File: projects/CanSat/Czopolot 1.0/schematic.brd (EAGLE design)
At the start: 35.6 x 50.8 mm, 12 parts

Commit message: Work work..
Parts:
- moved JP1 2.54 mm to (3.81, -48.3)
- moved JP2 2.54 mm to (36.8, -48.3)
- moved Q1 2.54 mm to (29.2, -49.5)
- moved Q2 2.54 mm to (11.4, -49.5)
- moved R1 2.54 mm to (29.2, -41.9)
- moved R2 2.54 mm to (11.4, -41.9)
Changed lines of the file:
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@@
 <?xml version="1.0" encoding="utf-8"?>
 <!DOCTYPE eagle SYSTEM "eagle.dtd">
-<eagle version="9.5.2">
+<eagle version="9.5.1">
 <drawing>
 <settings>
@@
 <element name="U$3" library="SobieskiSat2" package="MODULE_MPU9250" value="MPU9250" x="20.32" y="-8.001" smashed="yes" rot="R270"/>
 <element name="U$4" library="SobieskiSat2" package="MODULE_BMP280" value="BMP280" x="15.24" y="-28.829" smashed="yes" rot="R90"/>
-<element name="R1" library="rcl" library_urn="urn:adsk.eagle:library:334" package="0207/10" package3d_urn="urn:adsk.eagle:package:23491/2" value="" x="26.67" y="-41.91" smashed="yes" rot="R180">
-<attribute name="NAME" x="29.718" y="-43.434" size="1.27" layer="25" ratio="10" rot="R180"/>
-<attribute name="POPULARITY" value="81" x="26.67" y="-41.91" size="1.778" layer="27" rot="R180" display="off"/>
-<attribute name="SPICEPREFIX" value="R" x="26.67" y="-41.91" size="1.778" layer="27" rot="R180" display="off"/>
-<attribute name="VALUE" x="28.9306" y="-41.275" size="1.27" layer="27" ratio="10" rot="R180"/>
-</element>
-<element name="R2" library="rcl" library_urn="urn:adsk.eagle:library:334" package="0207/10" package3d_urn="urn:adsk.eagle:package:23491/2" value="" x="8.89" y="-41.91" smashed="yes" rot="R180">
-<attribute name="NAME" x="11.938" y="-43.434" size="1.27" layer="25" ratio="10" rot="R180"/>
-<attribute name="POPULARITY" value="81" x="8.89" y="-41.91" size="1.778" layer="27" rot="R180" display="off"/>
-<attribute name="SPICEPREFIX" value="R" x="8.89" y="-41.91" size="1.778" layer="27" rot="R180" display="off"/>
-<attribute name="VALUE" x="11.1506" y="-41.275" size="1.27" layer="27" ratio="10" rot="R180"/>
-</element>
-<element name="Q1" library="adafruit" library_urn="urn:adsk.eagle:library:420" package="TO220V" package3d_urn="urn:adsk.eagle:package:6240882/1" value="" x="26.67" y="-49.53" smashed="yes" rot="R180">
-<attribute name="NAME" x="31.75" y="-43.4848" size="1.27" layer="25" ratio="10" rot="R180"/>
-<attribute name="VALUE" x="31.75" y="-41.91" size="1.27" layer="27" ratio="10" rot="R180"/>
-</element>
-<element name="Q2" library="adafruit" library_urn="urn:adsk.eagle:library:420" package="TO220V" package3d_urn="urn:adsk.eagle:package:6240882/1" value="" x="8.89" y="-49.53" smashed="yes" rot="R180">
-<attribute name="NAME" x="13.97" y="-43.4848" size="1.27" layer="25" ratio="10" rot="R180"/>
-<attribute name="VALUE" x="13.97" y="-41.91" size="1.27" layer="27" ratio="10" rot="R180"/>
-</element>
-<element name="JP1" library="pinhead" library_urn="urn:adsk.eagle:library:325" package="1X02" package3d_urn="urn:adsk.eagle:package:22435/2" value="" x="1.27" y="-48.26" smashed="yes" rot="R90">
-<attribute name="NAME" x="-0.5588" y="-50.8762" size="1.27" layer="25" ratio="10" rot="R90"/>
-<attribute name="POPULARITY" value="98" x="1.27" y="-48.26" size="1.778" layer="27" rot="R90" display="off"/>
-<attribute name="VALUE" x="4.445" y="-50.8" size="1.27" layer="27" rot="R90"/>
-</element>
-<element name="JP2" library="pinhead" library_urn="urn:adsk.eagle:library:325" package="1X02" package3d_urn="urn:adsk.eagle:package:22435/2" value="" x="34.29" y="-48.26" smashed="yes" rot="R90">
-<attribute name="NAME" x="32.4612" y="-50.8762" size="1.27" layer="25" ratio="10" rot="R90"/>
-<attribute name="POPULARITY" value="98" x="34.29" y="-48.26" size="1.778" layer="27" rot="R90" display="off"/>
-<attribute name="VALUE" x="37.465" y="-50.8" size="1.27" layer="27" rot="R90"/>
+<element name="R1" library="rcl" library_urn="urn:adsk.eagle:library:334" package="0207/10" package3d_urn="urn:adsk.eagle:package:23491/2" value="" x="29.21" y="-41.91" smashed="yes" rot="R180">
+<attribute name="NAME" x="32.258" y="-43.434" size="1.27" layer="25" ratio="10" rot="R180"/>
+<attribute name="POPULARITY" value="81" x="29.21" y="-41.91" size="1.778" layer="27" rot="R180" display="off"/>
+<attribute name="SPICEPREFIX" value="R" x="29.21" y="-41.91" size="1.778" layer="27" rot="R180" display="off"/>
+<attribute name="VALUE" x="31.4706" y="-41.275" size="1.27" layer="27" ratio="10" rot="R180"/>
+</element>
+<element name="R2" library="rcl" library_urn="urn:adsk.eagle:library:334" package="0207/10" package3d_urn="urn:adsk.eagle:package:23491/2" value="" x="11.43" y="-41.91" smashed="yes" rot="R180">
+<attribute name="NAME" x="14.478" y="-43.434" size="1.27" layer="25" ratio="10" rot="R180"/>
+<attribute name="POPULARITY" value="81" x="11.43" y="-41.91" size="1.778" layer="27" rot="R180" display="off"/>
+<attribute name="SPICEPREFIX" value="R" x="11.43" y="-41.91" size="1.778" layer="27" rot="R180" display="off"/>
+<attribute name="VALUE" x="13.6906" y="-41.275" size="1.27" layer="27" ratio="10" rot="R180"/>
+</element>
+<element name="Q1" library="adafruit" library_urn="urn:adsk.eagle:library:420" package="TO220V" package3d_urn="urn:adsk.eagle:package:6240882/1" value="" x="29.21" y="-49.53" smashed="yes" rot="R180">
+<attribute name="NAME" x="34.29" y="-43.4848" size="1.27" layer="25" ratio="10" rot="R180"/>
+<attribute name="VALUE" x="34.29" y="-41.91" size="1.27" layer="27" ratio="10" rot="R180"/>
+</element>
+<element name="Q2" library="adafruit" library_urn="urn:adsk.eagle:library:420" package="TO220V" package3d_urn="urn:adsk.eagle:package:6240882/1" value="" x="11.43" y="-49.53" smashed="yes" rot="R180">
+<attribute name="NAME" x="16.51" y="-43.4848" size="1.27" layer="25" ratio="10" rot="R180"/>
+<attribute name="VALUE" x="16.51" y="-41.91" size="1.27" layer="27" ratio="10" rot="R180"/>
+</element>
+<element name="JP1" library="pinhead" library_urn="urn:adsk.eagle:library:325" package="1X02" package3d_urn="urn:adsk.eagle:package:22435/2" value="" x="3.81" y="-48.26" smashed="yes" rot="R90">
+<attribute name="NAME" x="1.9812" y="-50.8762" size="1.27" layer="25" ratio="10" rot="R90"/>
+<attribute name="POPULARITY" value="98" x="3.81" y="-48.26" size="1.778" layer="27" rot="R90" display="off"/>
+<attribute name="VALUE" x="6.985" y="-50.8" size="1.27" layer="27" rot="R90"/>
+</element>
+<element name="JP2" library="pinhead" library_urn="urn:adsk.eagle:library:325" package="1X02" package3d_urn="urn:adsk.eagle:package:22435/2" value="" x="36.83" y="-48.26" smashed="yes" rot="R90">
+<attribute name="NAME" x="35.0012" y="-50.8762" size="1.27" layer="25" ratio="10" rot="R90"/>
+<attribute name="POPULARITY" value="98" x="36.83" y="-48.26" size="1.778" layer="27" rot="R90" display="off"/>
+<attribute name="VALUE" x="40.005" y="-50.8" size="1.27" layer="27" rot="R90"/>
 </element>
 </elements>
@@
 <wire x1="3.81" y1="-3.81" x2="6.35" y2="-3.81" width="0" layer="19" extent="1-1"/>
 </signal>
-<signal name="GND">
+<signal name="GND" airwireshidden="yes">
 <contactref element="ULTIMATE_GPS" pad="2"/>
 <contactref element="U$2" pad="GND@1"/>
@@
 <wire x1="11.43" y1="-19.05" x2="17.13" y2="-23.51" width="0" layer="19" extent="1-1"/>
 </signal>
-<signal name="VCC">
+<signal name="VCC" airwireshidden="yes">
 <contactref element="U$2" pad="VCC"/>
 <contactref element="U$3" pad="VCC"/>
@@
 <wire x1="34.29" y1="-34.29" x2="31.13" y2="-23.51" width="0" layer="19" extent="1-1"/>
 </signal>
-<signal name="V+">
+<signal name="V+" airwireshidden="yes">
 <contactref element="U$1" pad="V+3"/>
 <contactref element="U$1" pad="V+2"/>

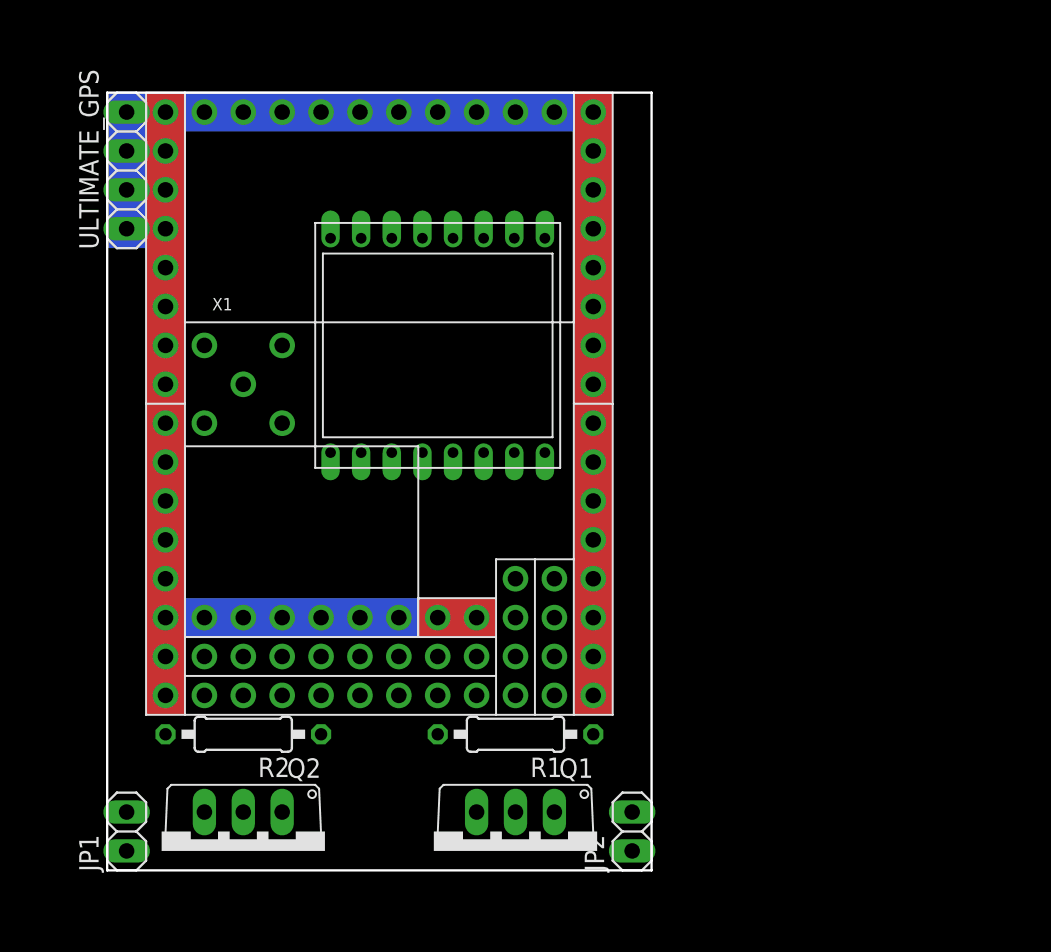
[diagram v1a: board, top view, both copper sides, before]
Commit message: Switch added
Duel switch and resistor added
Resistor type switched to another to match the grid
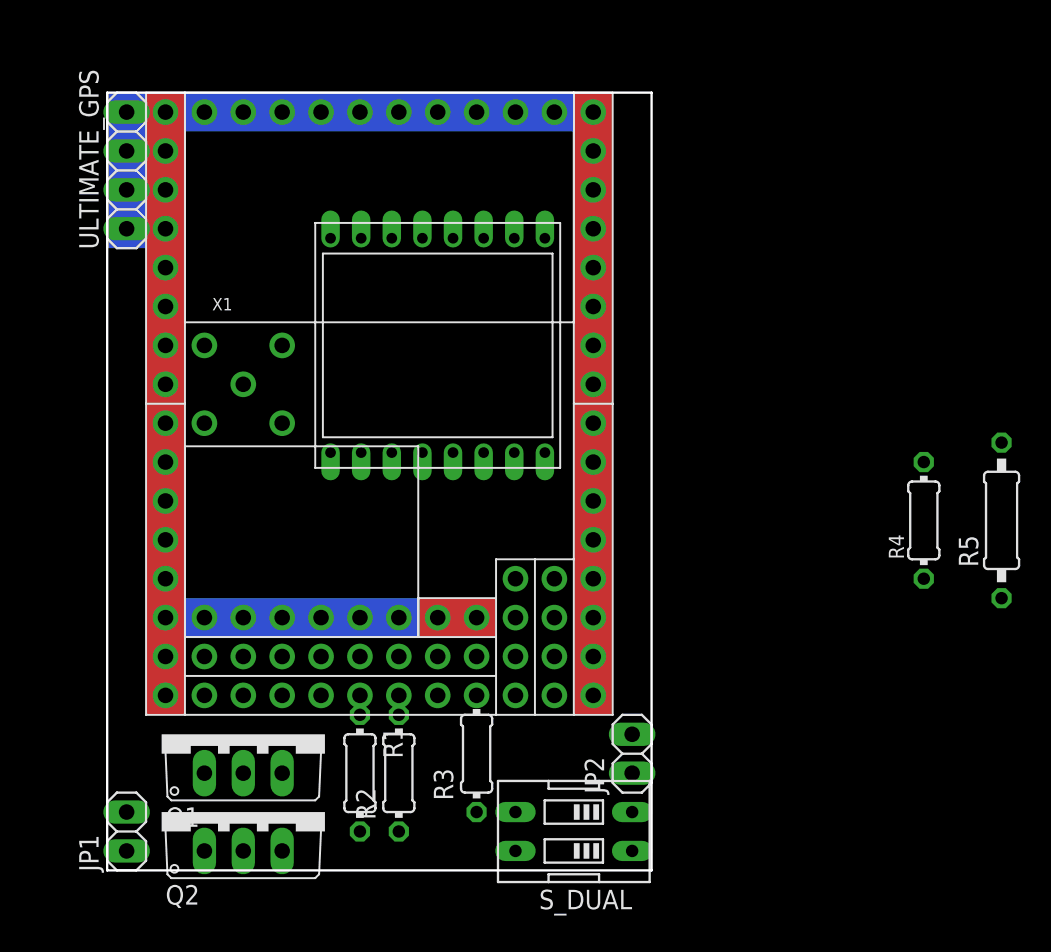
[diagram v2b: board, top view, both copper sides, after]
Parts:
- added R3: 4.7 k, rcl:0204/7
- added R4: (no value), rcl:0204/7
- added R5: (no value), rcl:0207/10
- added U$5: SWITCH_DUAL, SobieskiSat2:SWITCH_DUAL
- R1, R2: device rcl:0207/10 -> rcl:0204/7
- moved Q1 19.3 mm to (11.4, -41.9), turned to 0 degrees
- moved R1 10.5 mm to (19.1, -44.5), turned to 270 degrees
- moved R2 10.5 mm to (21.6, -44.5), turned to 90 degrees
- moved JP2 5.08 mm to (36.8, -43.2)
- moved Q2 2.54 mm to (11.4, -47.0), turned to 0 degrees
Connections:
- new net N$13: U$1.RST, U$1.RST1, U$5.4
- new net N$14: R3.1, U$1.X17, U$5.3
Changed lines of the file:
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@@
 <?xml version="1.0" encoding="utf-8"?>
 <!DOCTYPE eagle SYSTEM "eagle.dtd">
-<eagle version="9.5.1">
+<eagle version="9.5.2">
 <drawing>
 <settings>
@@
 <element name="U$3" library="SobieskiSat2" package="MODULE_MPU9250" value="MPU9250" x="20.32" y="-8.001" smashed="yes" rot="R270"/>
 <element name="U$4" library="SobieskiSat2" package="MODULE_BMP280" value="BMP280" x="15.24" y="-28.829" smashed="yes" rot="R90"/>
-<element name="R1" library="rcl" library_urn="urn:adsk.eagle:library:334" package="0207/10" package3d_urn="urn:adsk.eagle:package:23491/2" value="" x="29.21" y="-41.91" smashed="yes" rot="R180">
-<attribute name="NAME" x="32.258" y="-43.434" size="1.27" layer="25" ratio="10" rot="R180"/>
-<attribute name="POPULARITY" value="81" x="29.21" y="-41.91" size="1.778" layer="27" rot="R180" display="off"/>
-<attribute name="SPICEPREFIX" value="R" x="29.21" y="-41.91" size="1.778" layer="27" rot="R180" display="off"/>
-<attribute name="VALUE" x="31.4706" y="-41.275" size="1.27" layer="27" ratio="10" rot="R180"/>
-</element>
-<element name="R2" library="rcl" library_urn="urn:adsk.eagle:library:334" package="0207/10" package3d_urn="urn:adsk.eagle:package:23491/2" value="" x="11.43" y="-41.91" smashed="yes" rot="R180">
-<attribute name="NAME" x="14.478" y="-43.434" size="1.27" layer="25" ratio="10" rot="R180"/>
-<attribute name="POPULARITY" value="81" x="11.43" y="-41.91" size="1.778" layer="27" rot="R180" display="off"/>
-<attribute name="SPICEPREFIX" value="R" x="11.43" y="-41.91" size="1.778" layer="27" rot="R180" display="off"/>
-<attribute name="VALUE" x="13.6906" y="-41.275" size="1.27" layer="27" ratio="10" rot="R180"/>
-</element>
-<element name="Q1" library="adafruit" library_urn="urn:adsk.eagle:library:420" package="TO220V" package3d_urn="urn:adsk.eagle:package:6240882/1" value="" x="29.21" y="-49.53" smashed="yes" rot="R180">
-<attribute name="NAME" x="34.29" y="-43.4848" size="1.27" layer="25" ratio="10" rot="R180"/>
-<attribute name="VALUE" x="34.29" y="-41.91" size="1.27" layer="27" ratio="10" rot="R180"/>
-</element>
-<element name="Q2" library="adafruit" library_urn="urn:adsk.eagle:library:420" package="TO220V" package3d_urn="urn:adsk.eagle:package:6240882/1" value="" x="11.43" y="-49.53" smashed="yes" rot="R180">
-<attribute name="NAME" x="16.51" y="-43.4848" size="1.27" layer="25" ratio="10" rot="R180"/>
-<attribute name="VALUE" x="16.51" y="-41.91" size="1.27" layer="27" ratio="10" rot="R180"/>
+<element name="R1" library="rcl" library_urn="urn:adsk.eagle:library:334" package="0204/7" package3d_urn="urn:adsk.eagle:package:23498/2" value="" x="19.05" y="-44.45" smashed="yes" rot="R270">
+<attribute name="NAME" x="20.574" y="-41.402" size="1.27" layer="25" ratio="10" rot="R270"/>
+<attribute name="POPULARITY" value="79" x="19.05" y="-44.45" size="1.778" layer="27" rot="R270" display="off"/>
+<attribute name="SPICEPREFIX" value="R" x="19.05" y="-44.45" size="1.778" layer="27" rot="R270" display="off"/>
+<attribute name="VALUE" x="18.415" y="-42.1894" size="1.27" layer="27" ratio="10" rot="R270"/>
+</element>
+<element name="R2" library="rcl" library_urn="urn:adsk.eagle:library:334" package="0204/7" package3d_urn="urn:adsk.eagle:package:23498/2" value="" x="21.59" y="-44.45" smashed="yes" rot="R90">
+<attribute name="NAME" x="20.066" y="-47.498" size="1.27" layer="25" ratio="10" rot="R90"/>
+<attribute name="POPULARITY" value="79" x="21.59" y="-44.45" size="1.778" layer="27" rot="R90" display="off"/>
+<attribute name="SPICEPREFIX" value="R" x="21.59" y="-44.45" size="1.778" layer="27" rot="R90" display="off"/>
+<attribute name="VALUE" x="22.225" y="-46.7106" size="1.27" layer="27" ratio="10" rot="R90"/>
+</element>
+<element name="Q1" library="adafruit" library_urn="urn:adsk.eagle:library:420" package="TO220V" package3d_urn="urn:adsk.eagle:package:6240882/1" value="" x="11.43" y="-41.91" smashed="yes">
+<attribute name="NAME" x="6.35" y="-47.9552" size="1.27" layer="25" ratio="10"/>
+<attribute name="VALUE" x="6.35" y="-49.53" size="1.27" layer="27" ratio="10"/>
+</element>
+<element name="Q2" library="adafruit" library_urn="urn:adsk.eagle:library:420" package="TO220V" package3d_urn="urn:adsk.eagle:package:6240882/1" value="" x="11.43" y="-46.99" smashed="yes">
+<attribute name="NAME" x="6.35" y="-53.0352" size="1.27" layer="25" ratio="10"/>
+<attribute name="VALUE" x="6.35" y="-54.61" size="1.27" layer="27" ratio="10"/>
 </element>
 <element name="JP1" library="pinhead" library_urn="urn:adsk.eagle:library:325" package="1X02" package3d_urn="urn:adsk.eagle:package:22435/2" value="" x="3.81" y="-48.26" smashed="yes" rot="R90">
@@
 <attribute name="VALUE" x="6.985" y="-50.8" size="1.27" layer="27" rot="R90"/>
 </element>
-<element name="JP2" library="pinhead" library_urn="urn:adsk.eagle:library:325" package="1X02" package3d_urn="urn:adsk.eagle:package:22435/2" value="" x="36.83" y="-48.26" smashed="yes" rot="R90">
-<attribute name="NAME" x="35.0012" y="-50.8762" size="1.27" layer="25" ratio="10" rot="R90"/>
-<attribute name="POPULARITY" value="98" x="36.83" y="-48.26" size="1.778" layer="27" rot="R90" display="off"/>
-<attribute name="VALUE" x="40.005" y="-50.8" size="1.27" layer="27" rot="R90"/>
+<element name="JP2" library="pinhead" library_urn="urn:adsk.eagle:library:325" package="1X02" package3d_urn="urn:adsk.eagle:package:22435/2" value="" x="36.83" y="-43.18" smashed="yes" rot="R90">
+<attribute name="NAME" x="35.0012" y="-45.7962" size="1.27" layer="25" ratio="10" rot="R90"/>
+<attribute name="POPULARITY" value="98" x="36.83" y="-43.18" size="1.778" layer="27" rot="R90" display="off"/>
+<attribute name="VALUE" x="40.005" y="-45.72" size="1.27" layer="27" rot="R90"/>
+</element>
+<element name="U$5" library="SobieskiSat2" package="SWITCH_DUAL" value="SWITCH_DUAL" x="33.02" y="-48.26" smashed="yes" rot="R90"/>
+<element name="R3" library="rcl" library_urn="urn:adsk.eagle:library:334" package="0204/7" package3d_urn="urn:adsk.eagle:package:23498/2" value="4.7 k" x="26.67" y="-43.18" smashed="yes" rot="R90">
+<attribute name="NAME" x="25.146" y="-46.228" size="1.27" layer="25" ratio="10" rot="R90"/>
+<attribute name="POPULARITY" value="79" x="26.67" y="-43.18" size="1.778" layer="27" rot="R90" display="off"/>
+<attribute name="SPICEPREFIX" value="R" x="26.67" y="-43.18" size="1.778" layer="27" rot="R90" display="off"/>
+<attribute name="VALUE" x="27.305" y="-45.4406" size="1.27" layer="27" ratio="10" rot="R90"/>
+</element>
+<element name="R4" library="rcl" library_urn="urn:adsk.eagle:library:334" package="0204/7" package3d_urn="urn:adsk.eagle:package:23498/2" value="" x="55.88" y="-27.94" smashed="yes" rot="R90">
+<attribute name="NAME" x="54.5846" y="-30.48" size="0.9906" layer="25" ratio="10" rot="R90"/>
+<attribute name="POPULARITY" value="79" x="55.88" y="-27.94" size="1.778" layer="27" rot="R90" display="off"/>
+<attribute name="SPICEPREFIX" value="R" x="55.88" y="-27.94" size="1.778" layer="27" rot="R90" display="off"/>
+<attribute name="VALUE" x="56.3626" y="-29.5656" size="0.9906" layer="27" ratio="10" rot="R90"/>
+</element>
+<element name="R5" library="rcl" library_urn="urn:adsk.eagle:library:334" package="0207/10" package3d_urn="urn:adsk.eagle:package:23491/2" value="" x="60.96" y="-27.94" smashed="yes" rot="R90">
+<attribute name="NAME" x="59.436" y="-30.988" size="1.27" layer="25" ratio="10" rot="R90"/>
+<attribute name="POPULARITY" value="81" x="60.96" y="-27.94" size="1.778" layer="27" rot="R90" display="off"/>
+<attribute name="SPICEPREFIX" value="R" x="60.96" y="-27.94" size="1.778" layer="27" rot="R90" display="off"/>
+<attribute name="VALUE" x="61.595" y="-30.2006" size="1.27" layer="27" ratio="10" rot="R90"/>
 </element>
 </elements>
@@
 <wire x1="3.81" y1="-8.89" x2="6.35" y2="-39.37" width="0" layer="19" extent="1-1"/>
 </signal>
+<signal name="N$13">
+<contactref element="U$5" pad="4"/>
+<contactref element="U$1" pad="RST1"/>
+<contactref element="U$1" pad="RST"/>
+<wire x1="6.35" y1="-31.75" x2="34.29" y2="-8.89" width="0" layer="19" extent="1-1"/>
+<wire x1="29.21" y1="-49.53" x2="6.35" y2="-31.75" width="0" layer="19" extent="1-1"/>
+</signal>
+<signal name="N$14">
+<contactref element="U$5" pad="3"/>
+<contactref element="U$1" pad="X17"/>
+<contactref element="R3" pad="1"/>
+<wire x1="26.67" y1="-46.99" x2="8.89" y2="-39.37" width="0" layer="19" extent="1-1"/>
+<wire x1="29.21" y1="-46.99" x2="26.67" y2="-46.99" width="0" layer="19" extent="1-1"/>
+</signal>
 </signals>

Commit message: Added GND to switch
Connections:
- net GND: now also U$5.1, U$5.2
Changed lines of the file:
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@@
 <contactref element="U$4" pad="GND"/>
 <contactref element="U$3" pad="GND"/>
+<contactref element="U$5" pad="1"/>
+<contactref element="U$5" pad="2"/>
 <wire x1="25.13" y1="-9.51" x2="29.21" y2="-1.271" width="0" layer="19" extent="1-1"/>
 <wire x1="27.13" y1="-23.51" x2="25.13" y2="-9.51" width="0" layer="19" extent="1-1"/>
@@
 <wire x1="11.43" y1="-34.289" x2="19.13" y2="-23.51" width="0" layer="19" extent="1-1"/>
 <wire x1="3.81" y1="-6.35" x2="25.13" y2="-9.51" width="0" layer="19" extent="1-1"/>
+<wire x1="36.83" y1="-46.99" x2="27.13" y2="-23.51" width="0" layer="19" extent="1-1"/>
+<wire x1="36.83" y1="-49.53" x2="36.83" y2="-46.99" width="0" layer="19" extent="1-1"/>
 </signal>
 <signal name="N$1">
